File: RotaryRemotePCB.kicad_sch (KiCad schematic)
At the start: 10 parts, among them J1 Conn_01x02, J2 UART, J3 i2c, J4 Neopixel Connector, J5 EncoderRotary, J6 EncoderSwitch, SW1 RotaryEncoder_Switch, U1 TP4056, U2 WeMos_D1_mini

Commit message: Add git submodule
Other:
- moved on the sheet: BT1, U1
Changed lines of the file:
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@@
   (junction (at 205.994 86.106) (diameter 0) (color 0 0 0 0)
   )
+  (junction (at 135.128 56.642) (diameter 0) (color 0 0 0 0)
+  )
   (junction (at 230.632 86.106) (diameter 0) (color 0 0 0 0)
   )
@@
   (junction (at 230.632 91.186) (diameter 0) (color 0 0 0 0)
   )
-  (junction (at 130.81 51.562) (diameter 0) (color 0 0 0 0)
-  )
   (junction (at 205.994 91.186) (diameter 0) (color 0 0 0 0)
   )
+  (wire (pts (xy 135.128 56.642) (xy 126.746 56.642))
+    (stroke (width 0) (type default) (color 0 0 0 0))
+  )
   (wire (pts (xy 205.994 91.186) (xy 213.614 91.186))
     (stroke (width 0) (type default) (color 0 0 0 0))
@@
     (stroke (width 0) (type default) (color 0 0 0 0))
   )
-  (wire (pts (xy 154.686 43.688) (xy 156.718 43.688))
-    (stroke (width 0) (type default) (color 0 0 0 0))
-  )
   (wire (pts (xy 205.994 86.106) (xy 213.614 86.106))
     (stroke (width 0) (type default) (color 0 0 0 0))
@@
     (stroke (width 0) (type default) (color 0 0 0 0))
   )
-  (wire (pts (xy 126.746 51.562) (xy 126.746 47.752))
-    (stroke (width 0) (type default) (color 0 0 0 0))
-  )
   (wire (pts (xy 154.178 78.486) (xy 160.782 78.486))
     (stroke (width 0) (type default) (color 0 0 0 0))
@@
     (stroke (width 0) (type default) (color 0 0 0 0))
   )
-  (wire (pts (xy 154.686 49.022) (xy 154.686 51.308))
-    (stroke (width 0) (type default) (color 0 0 0 0))
-  )
-  (wire (pts (xy 154.686 45.212) (xy 154.686 43.688))
-    (stroke (width 0) (type default) (color 0 0 0 0))
-  )
   (wire (pts (xy 228.854 86.106) (xy 230.632 86.106))
     (stroke (width 0) (type default) (color 0 0 0 0))
@@
     (stroke (width 0) (type default) (color 0 0 0 0))
   )
-  (wire (pts (xy 134.366 45.212) (xy 134.366 42.672))
+  (wire (pts (xy 134.366 38.862) (xy 134.366 45.212))
     (stroke (width 0) (type default) (color 0 0 0 0))
   )
@@
     (stroke (width 0) (type default) (color 0 0 0 0))
   )
-  (wire (pts (xy 154.686 51.308) (xy 156.718 51.308))
+  (wire (pts (xy 144.526 38.862) (xy 134.366 38.862))
     (stroke (width 0) (type default) (color 0 0 0 0))
   )
@@
     (stroke (width 0) (type default) (color 0 0 0 0))
   )
-  (wire (pts (xy 134.366 51.562) (xy 130.81 51.562))
-    (stroke (width 0) (type default) (color 0 0 0 0))
-  )
-  (wire (pts (xy 130.81 51.562) (xy 126.746 51.562))
+  (wire (pts (xy 144.526 56.642) (xy 135.128 56.642))
+    (stroke (width 0) (type default) (color 0 0 0 0))
+  )
+  (wire (pts (xy 126.746 47.752) (xy 126.746 56.642))
     (stroke (width 0) (type default) (color 0 0 0 0))
   )
@@
     )
   )
-  (symbol (lib_id "power:GND") (at 130.81 51.562 0) (unit 1)
-    (in_bom yes) (on_board yes)
-    (property "Reference" "#PWR0101" (id 0) (at 130.81 57.912 0)
-      (effects (font (size 1.27 1.27)) hide)
-    )
-    (property "Value" "GND" (id 1) (at 130.81 58.674 90)
-      (effects (font (size 1.27 1.27)) (justify left))
-    )
-    (property "Footprint" "" (id 2) (at 130.81 51.562 0)
-      (effects (font (size 1.27 1.27)) hide)
-    )
-    (property "Datasheet" "" (id 3) (at 130.81 51.562 0)
+  (symbol (lib_id "power:GND") (at 135.128 56.642 0) (unit 1)
+    (in_bom yes) (on_board yes)
+    (property "Reference" "#PWR0101" (id 0) (at 135.128 62.992 0)
+      (effects (font (size 1.27 1.27)) hide)
+    )
+    (property "Value" "GND" (id 1) (at 135.128 63.754 90)
+      (effects (font (size 1.27 1.27)) (justify left))
+    )
+    (property "Footprint" "" (id 2) (at 135.128 56.642 0)
+      (effects (font (size 1.27 1.27)) hide)
+    )
+    (property "Datasheet" "" (id 3) (at 135.128 56.642 0)
       (effects (font (size 1.27 1.27)) hide)
     )
@@
     (pin "1")
   )
-  (symbol (lib_id "power:+5V") (at 154.686 41.402 270) (unit 1)
-    (in_bom yes) (on_board yes)
-    (property "Reference" "#PWR0106" (id 0) (at 150.876 41.402 0)
-      (effects (font (size 1.27 1.27)) hide)
-    )
-    (property "Value" "+5V" (id 1) (at 162.306 41.656 90)
+  (symbol (lib_id "power:+5V") (at 152.146 43.942 270) (unit 1)
+    (in_bom yes) (on_board yes)
+    (property "Reference" "#PWR0106" (id 0) (at 148.336 43.942 0)
+      (effects (font (size 1.27 1.27)) hide)
+    )
+    (property "Value" "+5V" (id 1) (at 159.766 44.196 90)
       (effects (font (size 1.27 1.27)) (justify right))
     )
-    (property "Footprint" "" (id 2) (at 154.686 41.402 0)
-      (effects (font (size 1.27 1.27)) hide)
-    )
-    (property "Datasheet" "" (id 3) (at 154.686 41.402 0)
+    (property "Footprint" "" (id 2) (at 152.146 43.942 0)
+      (effects (font (size 1.27 1.27)) hide)
+    )
+    (property "Datasheet" "" (id 3) (at 152.146 43.942 0)
       (effects (font (size 1.27 1.27)) hide)
     )
@@
     (pin "4")
   )
-  (symbol (lib_id "power:GND") (at 154.686 52.832 0) (unit 1)
-    (in_bom yes) (on_board yes)
-    (property "Reference" "#PWR0102" (id 0) (at 154.686 59.182 0)
-      (effects (font (size 1.27 1.27)) hide)
-    )
-    (property "Value" "GND" (id 1) (at 154.686 59.944 90)
-      (effects (font (size 1.27 1.27)) (justify left))
-    )
-    (property "Footprint" "" (id 2) (at 154.686 52.832 0)
-      (effects (font (size 1.27 1.27)) hide)
-    )
-    (property "Datasheet" "" (id 3) (at 154.686 52.832 0)
-      (effects (font (size 1.27 1.27)) hide)
-    )
-    (pin "1")
-  )
-  (symbol (lib_id "Device:Battery_Cell") (at 156.718 48.768 0) (unit 1)
-    (in_bom yes) (on_board yes) (fields_autoplaced)
-    (property "Reference" "BT1" (id 0) (at 160.782 45.4659 0)
-      (effects (font (size 1.27 1.27)) (justify left))
-    )
-    (property "Value" "Battery_Cell" (id 1) (at 160.782 48.0059 0)
-      (effects (font (size 1.27 1.27)) (justify left))
-    )
-    (property "Footprint" "Connector_PinHeader_2.54mm:PinHeader_1x02_P2.54mm_Vertical" (id 2) (at 156.718 47.244 90)
-      (effects (font (size 1.27 1.27)) hide)
-    )
-    (property "Datasheet" "~" (id 3) (at 156.718 47.244 90)
-      (effects (font (size 1.27 1.27)) hide)
-    )
+  (symbol (lib_id "power:GND") (at 152.146 51.562 90) (unit 1)
+    (in_bom yes) (on_board yes)
+    (property "Reference" "#PWR0102" (id 0) (at 158.496 51.562 0)
+      (effects (font (size 1.27 1.27)) hide)
+    )
+    (property "Value" "GND" (id 1) (at 159.258 51.562 90)
+      (effects (font (size 1.27 1.27)) (justify left))
+    )
+    (property "Footprint" "" (id 2) (at 152.146 51.562 0)
+      (effects (font (size 1.27 1.27)) hide)
+    )
+    (property "Datasheet" "" (id 3) (at 152.146 51.562 0)
+      (effects (font (size 1.27 1.27)) hide)
+    )
+    (pin "1")
+  )
+  (symbol (lib_id "Device:Battery_Cell") (at 136.906 49.022 0) (unit 1)
+    (in_bom yes) (on_board yes)
+    (property "Reference" "BT1" (id 0) (at 133.096 49.53 0)
+      (effects (font (size 1.27 1.27)) (justify left))
+    )
+    (property "Value" "Battery_Cell" (id 1) (at 140.97 48.2599 0)
+      (effects (font (size 1.27 1.27)) (justify left) hide)
+    )
+    (property "Footprint" "Connector_PinHeader_2.54mm:PinHeader_1x02_P2.54mm_Vertical" (id 2) (at 136.906 47.498 90)
+      (effects (font (size 1.27 1.27)) hide)
+    )
+    (property "Datasheet" "~" (id 3) (at 136.906 47.498 90)
+      (effects (font (size 1.27 1.27)) hide)
+    )

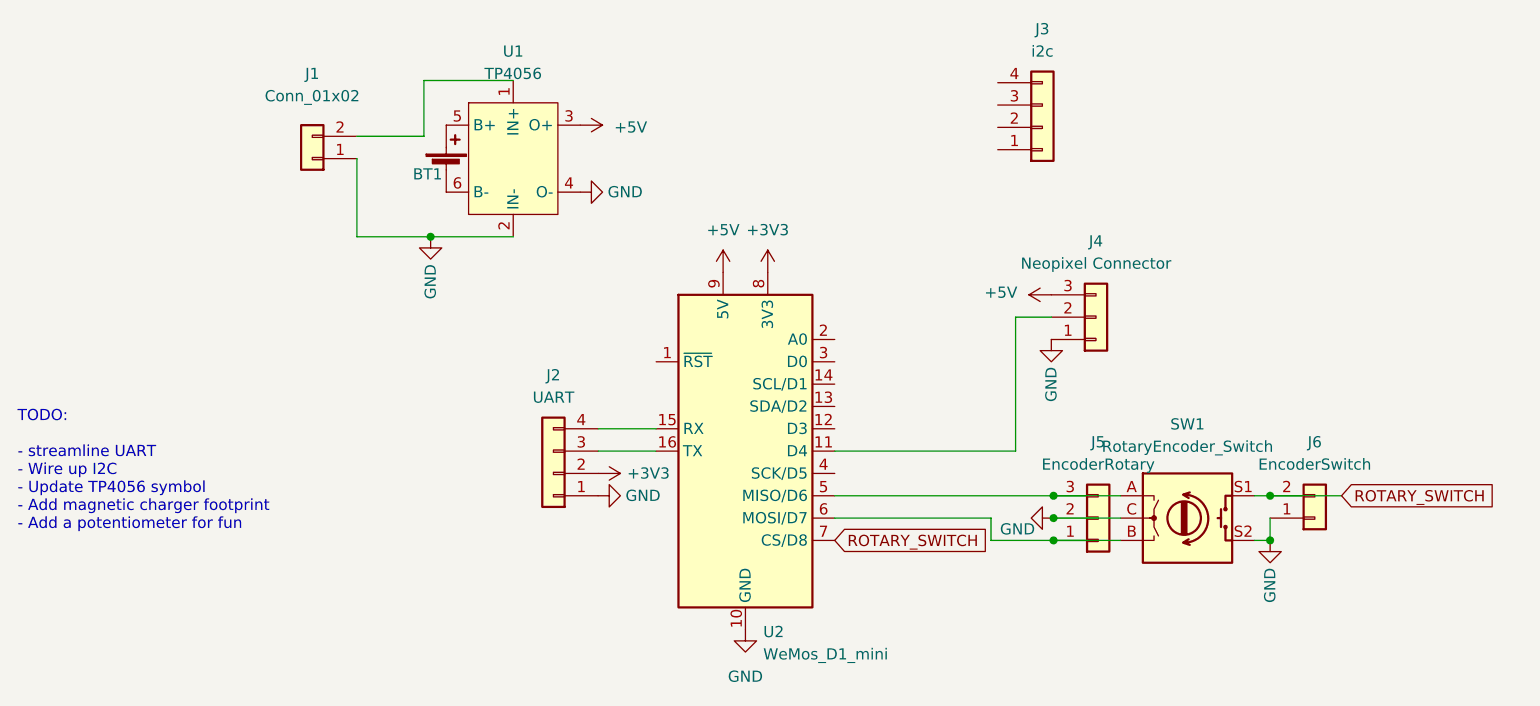
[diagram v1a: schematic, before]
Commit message: Add FTDI connector
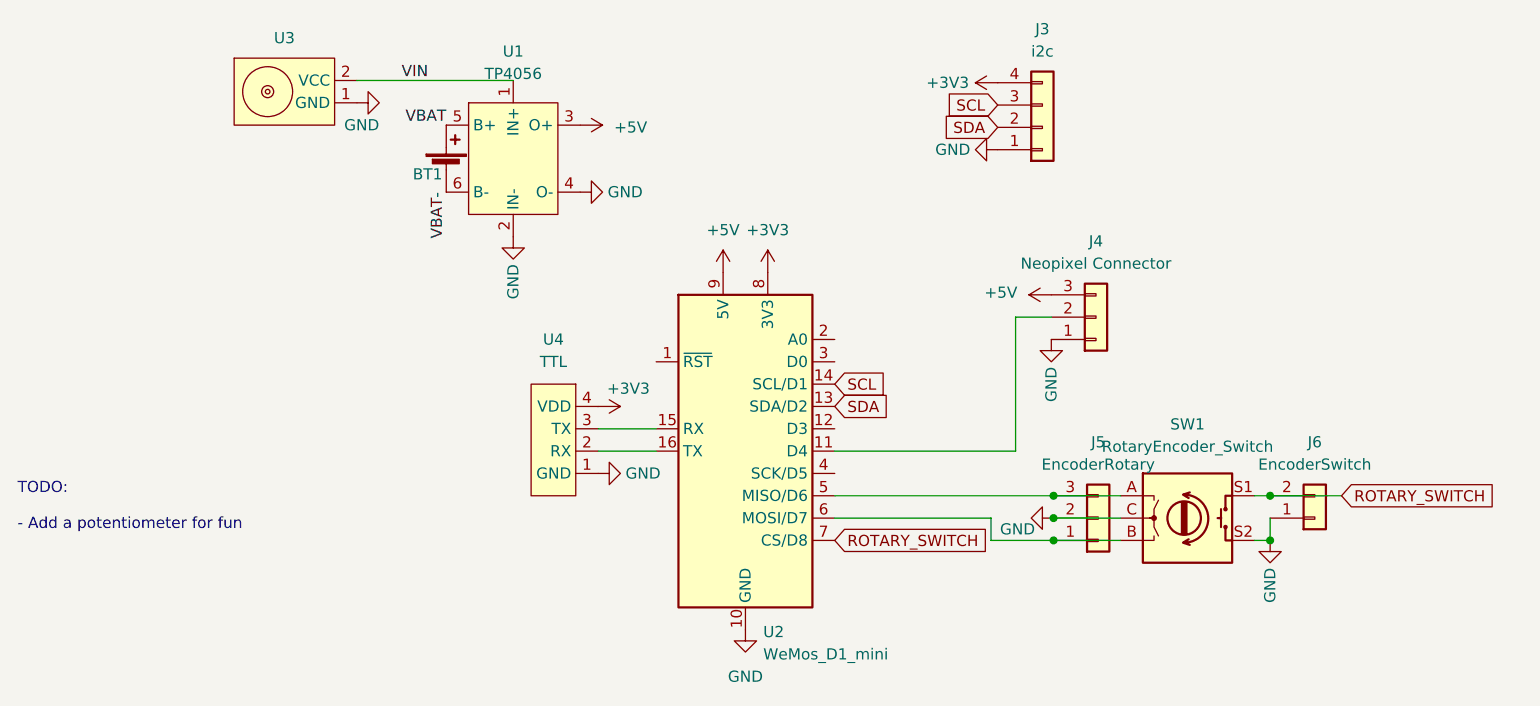
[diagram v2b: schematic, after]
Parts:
- removed J1: Conn_01x02, Connector_PinHeader_2.54mm:PinHeader_1x02_P2.54mm_Vertical, symbol Connector_Generic:Conn_01x02
- removed J2: UART, Connector_PinHeader_2.54mm:PinHeader_1x04_P2.54mm_Vertical, symbol Connector_Generic:Conn_01x04
- added U3: magnetic-charger, magnetic-charger:magnetic-charger, symbol magnetic-charger:magnetic-charger
- added U4: TTL, Connector_PinHeader_2.54mm:PinHeader_1x04_P2.54mm_Vertical, symbol ftdi-connector:TTL
- BT1: footprint Connector_PinHeader_2.54mm:PinHeader_1x02_P2.54mm_Vertical -> Connector_JST:JST_EH_S2B-EH_1x02_P2.50mm_Horizontal
- J4: footprint Connector_PinHeader_2.54mm:PinHeader_1x03_P2.54mm_Vertical -> Connector_PinHeader_2.54mm:PinHeader_1x03_P2.54mm_Horizontal
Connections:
- net +3V3: now also J3.4 (Pin_4), U4.4 (VDD)
- net GND: now also J3.1 (Pin_1), U3.1 (GND), U4.1 (GND)
- net VIN: now reaches U1.1 (IN+)
- net VIN: now also U3.2 (VCC)
- net SDA: now reaches J3.2 (Pin_2)
- net SDA: now also U2.13 (SDA/D2)
- net SCL: now reaches J3.3 (Pin_3)
- net SCL: now also U2.14 (SCL/D1)
- net at U2.16 (TX): now also U4.2 (RX)
- net at U2.15 (RX): now also U4.3 (TX)
- net VBAT: now reaches BT1.1 (+), U1.5 (B+)
- net VBAT-: now reaches BT1.2 (-), U1.6 (B-)
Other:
- note added: "TODO: - Add a potentiometer for fun"
- note removed: "TODO: - streamline UART - Wire up I2C - Update TP4056 symbol - Add magnetic charger footprint - Add a potentiometer for fun"
